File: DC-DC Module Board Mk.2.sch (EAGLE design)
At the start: 149 parts, among them U1 PCA9685, U3 LM1085IS-5.0

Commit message: finished vert molex microfit connectors
previous commit:
*vertical variant was corrected in PCB-Libraries prior to replacement*

fixed swapped pwm chan 2 and 0
THRUST2 in top left corner
PUMP (0) in next to last left corner
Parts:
- removed U$99: MOUNTINGHOLE2.5, microbuilder:MOUNTINGHOLE2.5
- UFIT1, UFIT3, UFIT5, UFIT7, UFITCAN: value MICRO-FIT-4-SMD-HZ -> MICRO-FIT-4-SMD-HZVT; device Connectors:MICRO-FIT-4-SMD-HZ -> Connectors:MICRO-FIT-4-SMD-HZVT
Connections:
- new net PMW3: UFIT3.P4
- net DGND: no longer UFIT4.P1, UFIT5.P1, UFIT6.P1
- net PWM1: now also UFIT1.P4
- net PWM2: now also UFIT0.P4
- net PWM4: now also UFIT4.P4
- net PWM5: now also UFIT5.P4
- net PWM6: now also UFIT6.P4
- net PWM7: now also UFIT7.P4
- net PWM8: now also UFIT8.P4
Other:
- note added: "pwm chan 0"
- note added: "thrust1"
- note added: "thrust2"
- note added: "thrust3"
- note added: "thrust4"
- note added: "thrust5"
- note added: "thrust6"
- note added: "thrust7"
- note added: "thrust8"
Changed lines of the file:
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@@
 <part name="GND39" library="supply1" deviceset="GND" device=""/>
 <part name="UFIT0" library="Connectors" deviceset="MICRO-FIT-4-SMD-HZ" device="VT" value="MICRO-FIT-4-SMD-HZVT"/>
-<part name="UFIT1" library="Connectors" deviceset="MICRO-FIT-4-SMD-HZ" device=""/>
+<part name="UFIT1" library="Connectors" deviceset="MICRO-FIT-4-SMD-HZ" device="VT" value="MICRO-FIT-4-SMD-HZVT"/>
 <part name="UFIT6" library="Connectors" deviceset="MICRO-FIT-4-SMD-HZ" device="VT" value="MICRO-FIT-4-SMD-HZVT"/>
-<part name="UFIT5" library="Connectors" deviceset="MICRO-FIT-4-SMD-HZ" device=""/>
+<part name="UFIT5" library="Connectors" deviceset="MICRO-FIT-4-SMD-HZ" device="VT" value="MICRO-FIT-4-SMD-HZVT"/>
 <part name="UFIT4" library="Connectors" deviceset="MICRO-FIT-4-SMD-HZ" device="VT" value="MICRO-FIT-4-SMD-HZVT"/>
-<part name="UFIT3" library="Connectors" deviceset="MICRO-FIT-4-SMD-HZ" device=""/>
-<part name="UFIT7" library="Connectors" deviceset="MICRO-FIT-4-SMD-HZ" device=""/>
+<part name="UFIT3" library="Connectors" deviceset="MICRO-FIT-4-SMD-HZ" device="VT" value="MICRO-FIT-4-SMD-HZVT"/>
+<part name="UFIT7" library="Connectors" deviceset="MICRO-FIT-4-SMD-HZ" device="VT" value="MICRO-FIT-4-SMD-HZVT"/>
 <part name="UFIT8" library="Connectors" deviceset="MICRO-FIT-4-SMD-HZ" device="VT" value="MICRO-FIT-4-SMD-HZVT"/>
 <part name="UFITTUBE" library="Connectors" deviceset="MICRO-FIT-4-SMD-HZ" device="VT" value="MICRO-FIT-4-SMD-HZVT"/>
@@
 <part name="R22" library="rcl" deviceset="R-US_" device="R0603" value="120"/>
 <part name="R17" library="rcl" deviceset="R-US_" device="R0603" value="120"/>
-<part name="UFITCAN" library="Connectors" deviceset="MICRO-FIT-4-SMD-HZ" device=""/>
+<part name="UFITCAN" library="Connectors" deviceset="MICRO-FIT-4-SMD-HZ" device="VT" value="MICRO-FIT-4-SMD-HZVT"/>
 <part name="U$12" library="DiscreteComponents" deviceset="BSS138" device=""/>
 <part name="R18" library="rcl" deviceset="R-US_" device="R0603" value="10K"/>
@@
 <part name="P+12" library="microbuilder" deviceset="VCC" device=""/>
 <part name="P+13" library="microbuilder" deviceset="VCC" device=""/>
-<part name="U$99" library="microbuilder" deviceset="MOUNTINGHOLE" device="2.5"/>
 <part name="U$100" library="microbuilder" deviceset="MOUNTINGHOLE" device="2.5"/>
 <part name="U$101" library="microbuilder" deviceset="MOUNTINGHOLE" device="2.5"/>
@@
 <text x="-236.22" y="-60.96" size="1.778" layer="97">I2C Address =</text>
 <text x="-243.84" y="-68.58" size="1.778" layer="97">Open = 0 / Closed = 1</text>
+<text x="330.2" y="175.26" size="1.778" layer="95">thrust2</text>
+<text x="330.2" y="195.58" size="1.778" layer="95">thrust1</text>
+<text x="330.2" y="154.94" size="1.778" layer="95">thrust3</text>
+<text x="330.2" y="134.62" size="1.778" layer="95">thrust4</text>
+<text x="330.2" y="114.3" size="1.778" layer="95">thrust5</text>
+<text x="330.2" y="93.98" size="1.778" layer="95">thrust6</text>
+<text x="330.2" y="73.66" size="1.778" layer="95">thrust7</text>
+<text x="330.2" y="53.34" size="1.778" layer="95">thrust8</text>
+<text x="441.96" y="172.72" size="1.778" layer="95">pwm chan 0</text>
 </plain>
 <instances>
@@
 <attribute name="NAME" x="68.58" y="71.12" size="1.778" layer="95"/>
 </instance>
-<instance part="UFIT0" gate="G$1" x="314.96" y="193.04" rot="R270"/>
-<instance part="UFIT1" gate="G$1" x="314.96" y="172.72" rot="R270"/>
-<instance part="UFIT6" gate="G$1" x="314.96" y="152.4" rot="R270"/>
-<instance part="UFIT5" gate="G$1" x="314.96" y="132.08" rot="R270"/>
-<instance part="UFIT4" gate="G$1" x="314.96" y="111.76" rot="R270"/>
-<instance part="UFIT3" gate="G$1" x="314.96" y="91.44" rot="R270"/>
+<instance part="UFIT0" gate="G$1" x="314.96" y="172.72" rot="R270"/>
+<instance part="UFIT1" gate="G$1" x="314.96" y="193.04" rot="R270"/>
+<instance part="UFIT6" gate="G$1" x="314.96" y="91.44" rot="R270"/>
+<instance part="UFIT5" gate="G$1" x="314.96" y="111.76" rot="R270"/>
+<instance part="UFIT4" gate="G$1" x="314.96" y="132.08" rot="R270"/>
+<instance part="UFIT3" gate="G$1" x="314.96" y="152.4" rot="R270"/>
 <instance part="UFIT7" gate="G$1" x="314.96" y="71.12" rot="R270"/>
 <instance part="UFIT8" gate="G$1" x="314.96" y="50.8" rot="R270"/>
@@
 <instance part="P+12" gate="VCC" x="-220.98" y="-167.64"/>
 <instance part="P+13" gate="VCC" x="-228.6" y="-167.64"/>
-<instance part="U$99" gate="G$1" x="-17.78" y="-187.96"/>
 <instance part="U$100" gate="G$1" x="-22.86" y="-187.96"/>
 <instance part="U$101" gate="G$1" x="-27.94" y="-187.96"/>
@@
 <segment>
 <pinref part="UFIT0" gate="G$1" pin="P1"/>
+<wire x1="322.58" y1="165.1" x2="327.66" y2="165.1" width="0.1524" layer="91"/>
+<label x="327.66" y="165.1" size="1.27" layer="95" xref="yes"/>
+</segment>
+<segment>
+<pinref part="UFIT1" gate="G$1" pin="P1"/>
 <wire x1="322.58" y1="185.42" x2="327.66" y2="185.42" width="0.1524" layer="91"/>
 <label x="327.66" y="185.42" size="1.27" layer="95" xref="yes"/>
 </segment>
 <segment>
-<pinref part="UFIT1" gate="G$1" pin="P1"/>
-<wire x1="322.58" y1="165.1" x2="327.66" y2="165.1" width="0.1524" layer="91"/>
-<label x="327.66" y="165.1" size="1.27" layer="95" xref="yes"/>
-</segment>
-<segment>
-<pinref part="UFIT6" gate="G$1" pin="P1"/>
+<pinref part="UFIT3" gate="G$1" pin="P1"/>
 <wire x1="322.58" y1="144.78" x2="327.66" y2="144.78" width="0.1524" layer="91"/>
 <label x="327.66" y="144.78" size="1.27" layer="95" xref="yes"/>
-</segment>
-<segment>
-<pinref part="UFIT5" gate="G$1" pin="P1"/>
-<wire x1="322.58" y1="124.46" x2="327.66" y2="124.46" width="0.1524" layer="91"/>
-<label x="327.66" y="124.46" size="1.27" layer="95" xref="yes"/>
-</segment>
-<segment>
-<pinref part="UFIT4" gate="G$1" pin="P1"/>
-<wire x1="322.58" y1="104.14" x2="327.66" y2="104.14" width="0.1524" layer="91"/>
-<label x="327.66" y="104.14" size="1.27" layer="95" xref="yes"/>
-</segment>
-<segment>
-<pinref part="UFIT3" gate="G$1" pin="P1"/>
-<wire x1="322.58" y1="83.82" x2="327.66" y2="83.82" width="0.1524" layer="91"/>
-<label x="327.66" y="83.82" size="1.27" layer="95" xref="yes"/>
 </segment>
 <segment>
@@
 <wire x1="246.38" y1="-35.56" x2="251.46" y2="-35.56" width="0.1524" layer="91"/>
 <label x="246.38" y="-35.56" size="1.778" layer="95"/>
+</segment>
+<segment>
+<wire x1="322.58" y1="124.46" x2="327.66" y2="124.46" width="0.1524" layer="91"/>
+<label x="327.66" y="124.46" size="1.27" layer="95" xref="yes"/>
+</segment>
+<segment>
+<wire x1="322.58" y1="104.14" x2="327.66" y2="104.14" width="0.1524" layer="91"/>
+<label x="327.66" y="104.14" size="1.27" layer="95" xref="yes"/>
+</segment>
+<segment>
+<wire x1="322.58" y1="83.82" x2="327.66" y2="83.82" width="0.1524" layer="91"/>
+<label x="327.66" y="83.82" size="1.27" layer="95" xref="yes"/>
 </segment>
 </net>
@@
 <pinref part="RPWM1" gate="G$1" pin="2"/>
 </segment>
+<segment>
+<pinref part="UFIT1" gate="G$1" pin="P4"/>
+<wire x1="322.58" y1="200.66" x2="327.66" y2="200.66" width="0.1524" layer="91"/>
+<label x="327.66" y="200.66" size="1.778" layer="95"/>
+</segment>
 </net>
 <net name="PWM2" class="0">
@@
 <pinref part="RPWM2" gate="G$1" pin="2"/>
 </segment>
+<segment>
+<pinref part="UFIT0" gate="G$1" pin="P4"/>
+<wire x1="322.58" y1="180.34" x2="327.66" y2="180.34" width="0.1524" layer="91"/>
+<label x="327.66" y="180.34" size="1.778" layer="95"/>
+</segment>
 </net>
 <net name="PWM3" class="0">
@@
 <pinref part="RPWM4" gate="G$1" pin="2"/>
 </segment>
+<segment>
+<pinref part="UFIT4" gate="G$1" pin="P4"/>
+<wire x1="322.58" y1="139.7" x2="327.66" y2="139.7" width="0.1524" layer="91"/>
+<label x="327.66" y="139.7" size="1.778" layer="95"/>
+</segment>
 </net>
 <net name="PWM5" class="0">
@@
 <label x="-101.6" y="-73.66" size="1.778" layer="95"/>
 <pinref part="RPWM5" gate="G$1" pin="2"/>
+</segment>
+<segment>
+<pinref part="UFIT5" gate="G$1" pin="P4"/>
+<wire x1="322.58" y1="119.38" x2="327.66" y2="119.38" width="0.1524" layer="91"/>
+<label x="327.66" y="119.38" size="1.778" layer="95"/>
 </segment>
 </net>
@@
 <pinref part="RPWM6" gate="G$1" pin="2"/>
 </segment>
+<segment>
+<pinref part="UFIT6" gate="G$1" pin="P4"/>
+<wire x1="322.58" y1="99.06" x2="327.66" y2="99.06" width="0.1524" layer="91"/>
+<label x="327.66" y="99.06" size="1.778" layer="95"/>
+</segment>
 </net>
 <net name="PWM7" class="0">
@@
 <pinref part="RPWM7" gate="G$1" pin="2"/>
 </segment>
+<segment>
+<pinref part="UFIT7" gate="G$1" pin="P4"/>
+<wire x1="322.58" y1="78.74" x2="327.66" y2="78.74" width="0.1524" layer="91"/>
+<label x="327.66" y="78.74" size="1.778" layer="95"/>
+</segment>
 </net>
 <net name="PWM8" class="0">
@@
 <label x="-60.96" y="-93.98" size="1.778" layer="95"/>
 <pinref part="RPWM8" gate="G$1" pin="2"/>
+</segment>
+<segment>
+<pinref part="UFIT8" gate="G$1" pin="P4"/>
+<wire x1="322.58" y1="58.42" x2="327.66" y2="58.42" width="0.1524" layer="91"/>
+<label x="327.66" y="58.42" size="1.778" layer="95"/>
 </segment>
 </net>
@@
 </segment>
 </net>
+<net name="PMW3" class="0">
+<segment>
+<pinref part="UFIT3" gate="G$1" pin="P4"/>
+<wire x1="322.58" y1="160.02" x2="327.66" y2="160.02" width="0.1524" layer="91"/>
+<label x="327.66" y="160.02" size="1.778" layer="95"/>
+</segment>
+</net>

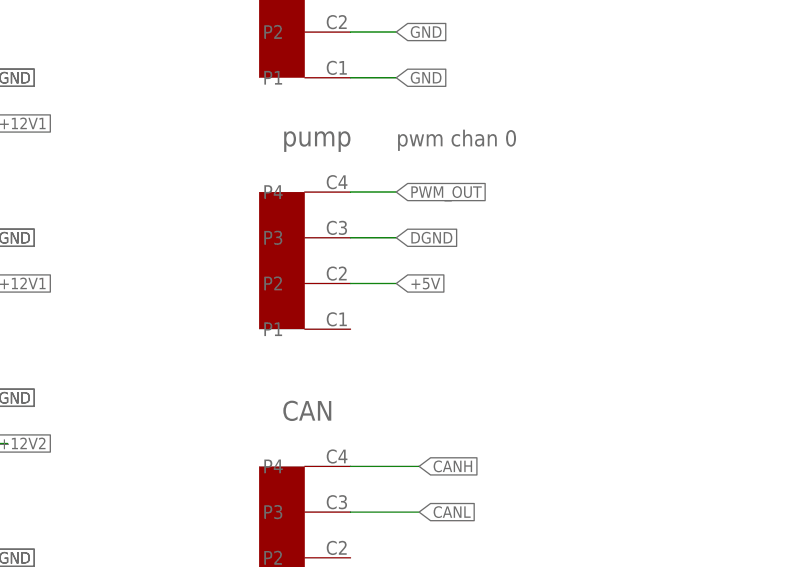
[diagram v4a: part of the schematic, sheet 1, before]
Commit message: laying out pwm chip
also removed +5V from pump
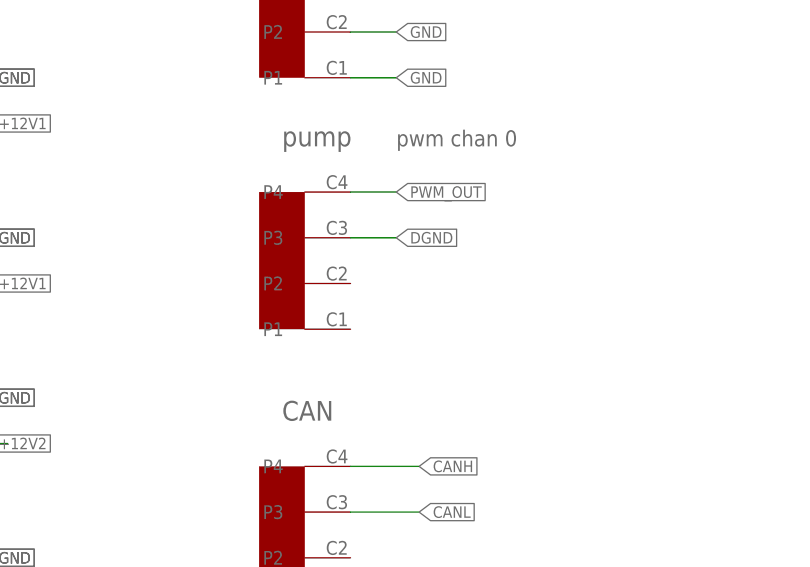
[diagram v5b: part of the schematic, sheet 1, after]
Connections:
- net +5V: no longer UFIT2.P2
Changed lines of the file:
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@@
 <grid distance="0.1" unitdist="inch" unit="inch" style="lines" multiple="1" display="no" altdistance="0.01" altunitdist="inch" altunit="inch"/>
 <layers>
-<layer number="1" name="Top" color="4" fill="1" visible="yes" active="no"/>
-<layer number="2" name="Route2" color="1" fill="3" visible="yes" active="no"/>
-<layer number="3" name="Route3" color="4" fill="3" visible="yes" active="no"/>
-<layer number="4" name="Route4" color="1" fill="4" visible="yes" active="no"/>
-<layer number="5" name="Route5" color="4" fill="4" visible="yes" active="no"/>
-<layer number="6" name="Route6" color="1" fill="8" visible="yes" active="no"/>
-<layer number="7" name="Route7" color="4" fill="8" visible="yes" active="no"/>
-<layer number="8" name="Route8" color="1" fill="2" visible="yes" active="no"/>
-<layer number="9" name="Route9" color="4" fill="2" visible="yes" active="no"/>
-<layer number="10" name="Route10" color="1" fill="7" visible="yes" active="no"/>
-<layer number="11" name="Route11" color="4" fill="7" visible="yes" active="no"/>
-<layer number="12" name="Route12" color="1" fill="5" visible="yes" active="no"/>
-<layer number="13" name="Route13" color="4" fill="5" visible="yes" active="no"/>
-<layer number="14" name="Route14" color="1" fill="6" visible="yes" active="no"/>
-<layer number="15" name="Route15" color="4" fill="6" visible="yes" active="no"/>
-<layer number="16" name="Bottom" color="1" fill="1" visible="yes" active="no"/>
-<layer number="17" name="Pads" color="2" fill="1" visible="yes" active="no"/>
-<layer number="18" name="Vias" color="2" fill="1" visible="yes" active="no"/>
-<layer number="19" name="Unrouted" color="6" fill="1" visible="yes" active="no"/>
-<layer number="20" name="Dimension" color="15" fill="1" visible="yes" active="no"/>
-<layer number="21" name="tPlace" color="7" fill="1" visible="yes" active="no"/>
-<layer number="22" name="bPlace" color="13" fill="1" visible="yes" active="no"/>
-<layer number="23" name="tOrigins" color="15" fill="1" visible="yes" active="no"/>
-<layer number="24" name="bOrigins" color="13" fill="1" visible="yes" active="no"/>
-<layer number="25" name="tNames" color="7" fill="1" visible="yes" active="no"/>
-<layer number="26" name="bNames" color="7" fill="1" visible="yes" active="no"/>
-<layer number="27" name="tValues" color="7" fill="1" visible="yes" active="no"/>
-<layer number="28" name="bValues" color="7" fill="1" visible="yes" active="no"/>
+<layer number="1" name="Top" color="4" fill="1" visible="no" active="no"/>
+<layer number="2" name="Route2" color="1" fill="3" visible="no" active="no"/>
+<layer number="3" name="Route3" color="4" fill="3" visible="no" active="no"/>
+<layer number="4" name="Route4" color="1" fill="4" visible="no" active="no"/>
+<layer number="5" name="Route5" color="4" fill="4" visible="no" active="no"/>
+<layer number="6" name="Route6" color="1" fill="8" visible="no" active="no"/>
+<layer number="7" name="Route7" color="4" fill="8" visible="no" active="no"/>
+<layer number="8" name="Route8" color="1" fill="2" visible="no" active="no"/>
+<layer number="9" name="Route9" color="4" fill="2" visible="no" active="no"/>
+<layer number="10" name="Route10" color="1" fill="7" visible="no" active="no"/>
+<layer number="11" name="Route11" color="4" fill="7" visible="no" active="no"/>
+<layer number="12" name="Route12" color="1" fill="5" visible="no" active="no"/>
+<layer number="13" name="Route13" color="4" fill="5" visible="no" active="no"/>
+<layer number="14" name="Route14" color="1" fill="6" visible="no" active="no"/>
+<layer number="15" name="Route15" color="4" fill="6" visible="no" active="no"/>
+<layer number="16" name="Bottom" color="1" fill="1" visible="no" active="no"/>
+<layer number="17" name="Pads" color="2" fill="1" visible="no" active="no"/>
+<layer number="18" name="Vias" color="2" fill="1" visible="no" active="no"/>
+<layer number="19" name="Unrouted" color="6" fill="1" visible="no" active="no"/>
+<layer number="20" name="Dimension" color="15" fill="1" visible="no" active="no"/>
+<layer number="21" name="tPlace" color="7" fill="1" visible="no" active="no"/>
+<layer number="22" name="bPlace" color="13" fill="1" visible="no" active="no"/>
+<layer number="23" name="tOrigins" color="15" fill="1" visible="no" active="no"/>
+<layer number="24" name="bOrigins" color="13" fill="1" visible="no" active="no"/>
+<layer number="25" name="tNames" color="7" fill="1" visible="no" active="no"/>
+<layer number="26" name="bNames" color="7" fill="1" visible="no" active="no"/>
+<layer number="27" name="tValues" color="7" fill="1" visible="no" active="no"/>
+<layer number="28" name="bValues" color="7" fill="1" visible="no" active="no"/>
 <layer number="29" name="tStop" color="7" fill="3" visible="no" active="no"/>
 <layer number="30" name="bStop" color="7" fill="6" visible="no" active="no"/>
@@
 <layer number="35" name="tGlue" color="7" fill="4" visible="no" active="no"/>
 <layer number="36" name="bGlue" color="7" fill="5" visible="no" active="no"/>
-<layer number="37" name="tTest" color="7" fill="1" visible="yes" active="no"/>
-<layer number="38" name="bTest" color="7" fill="1" visible="yes" active="no"/>
+<layer number="37" name="tTest" color="7" fill="1" visible="no" active="no"/>
+<layer number="38" name="bTest" color="7" fill="1" visible="no" active="no"/>
 <layer number="39" name="tKeepout" color="4" fill="11" visible="no" active="no"/>
 <layer number="40" name="bKeepout" color="1" fill="11" visible="no" active="no"/>
@@
 <layer number="44" name="Drills" color="7" fill="1" visible="no" active="no"/>
 <layer number="45" name="Holes" color="7" fill="1" visible="no" active="no"/>
-<layer number="46" name="Milling" color="3" fill="1" visible="yes" active="no"/>
-<layer number="47" name="Measures" color="7" fill="1" visible="yes" active="no"/>
-<layer number="48" name="Document" color="7" fill="1" visible="yes" active="no"/>
-<layer number="49" name="Reference" color="7" fill="1" visible="yes" active="no"/>
-<layer number="50" name="dxf" color="7" fill="1" visible="yes" active="no"/>
-<layer number="51" name="tDocu" color="14" fill="1" visible="yes" active="no"/>
-<layer number="52" name="bDocu" color="7" fill="1" visible="yes" active="no"/>
-<layer number="53" name="tGND_GNDA" color="7" fill="9" visible="yes" active="no"/>
-<layer number="54" name="bGND_GNDA" color="1" fill="9" visible="yes" active="no"/>
-<layer number="56" name="wert" color="7" fill="1" visible="yes" active="no"/>
-<layer number="57" name="tCAD" color="7" fill="1" visible="yes" active="no"/>
-<layer number="59" name="tCarbon" color="7" fill="1" visible="yes" active="no"/>
-<layer number="60" name="bCarbon" color="7" fill="1" visible="yes" active="no"/>
+<layer number="46" name="Milling" color="3" fill="1" visible="no" active="no"/>
+<layer number="47" name="Measures" color="7" fill="1" visible="no" active="no"/>
+<layer number="48" name="Document" color="7" fill="1" visible="no" active="no"/>
+<layer number="49" name="Reference" color="7" fill="1" visible="no" active="no"/>
+<layer number="50" name="dxf" color="7" fill="1" visible="no" active="no"/>
+<layer number="51" name="tDocu" color="14" fill="1" visible="no" active="no"/>
+<layer number="52" name="bDocu" color="7" fill="1" visible="no" active="no"/>
+<layer number="53" name="tGND_GNDA" color="7" fill="9" visible="no" active="no"/>
+<layer number="54" name="bGND_GNDA" color="1" fill="9" visible="no" active="no"/>
+<layer number="56" name="wert" color="7" fill="1" visible="no" active="no"/>
+<layer number="57" name="tCAD" color="7" fill="1" visible="no" active="no"/>
+<layer number="59" name="tCarbon" color="7" fill="1" visible="no" active="no"/>
+<layer number="60" name="bCarbon" color="7" fill="1" visible="no" active="no"/>
 <layer number="90" name="Modules" color="5" fill="1" visible="yes" active="yes"/>
 <layer number="91" name="Nets" color="2" fill="1" visible="yes" active="yes"/>
@@
 </segment>
 <segment>
-<pinref part="UFIT2" gate="G$1" pin="P2"/>
-<wire x1="436.88" y1="157.48" x2="441.96" y2="157.48" width="0.1524" layer="91"/>
-<label x="441.96" y="157.48" size="1.27" layer="95" xref="yes"/>
-</segment>
-<segment>
